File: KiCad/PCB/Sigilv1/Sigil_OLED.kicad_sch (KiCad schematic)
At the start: 13 parts, among them J2 INLAND 1.3" OLED HEADER (7-PI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, J3 BUZZER 2-PIN HEADER, J5 STATUS RING CABLE (JST-XH 3), SW1 UP (GPIO25, J11), SW2 DOWN (GPIO27, J9), SW3 LEFT (GPIO19, A12), SW4 RIGHT (GPIO21, A14), SW5 SELECT (GPIO32, J13), U1 REMOVABLE ESP32 DEVKIT / 2 x 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, U2 74AHCT1G125

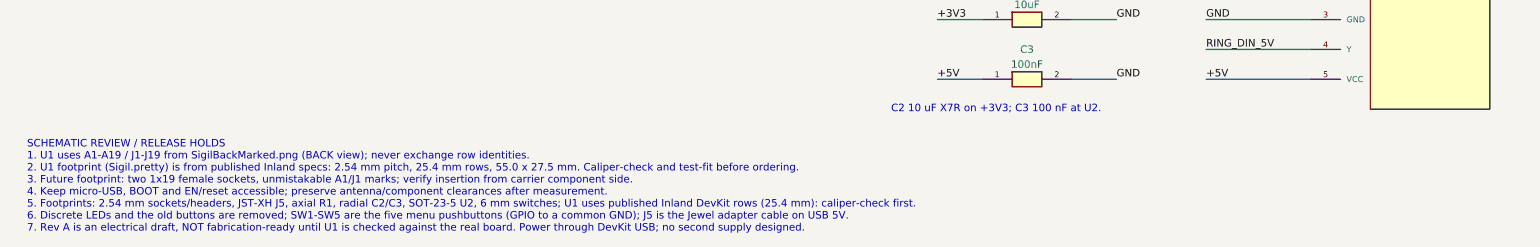
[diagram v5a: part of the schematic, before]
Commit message: Sigil U1 footprint: rows 22.86 mm, WROOM-32E, antenna keep-out
- The owner's Sigil DevKit straddles a standard breadboard with one free
  hole outside each row (columns b and i), so its rows are 22.86 mm
  (0.9 in) apart, not the published 25.4 mm. The footprint is renamed
  ESP32_DevKit_38_Socket_Row22.86mm; the 25.4 mm board is the wider
  30-pin DevKit on the test harness.
- Description names the ESP32-WROOM-32E module the boards actually carry.
- New 7 mm keep-out (no tracks, vias, pours or parts; socket pads allowed)
  over the antenna end past A19/J19. The depth is an estimate: measure it.
- Schematic release notes, README, CROSS_CHECK and the Prototype 1.0 gap
  review updated. KiCad 10.0.6 ERC: 0 violations on all three schematics;
  verify_schematic.py passes on exported netlists. Still Needs verification
  with calipers before ordering.

Co-Authored-By: Claude Opus 5.5 <noreply@anthropic.com>
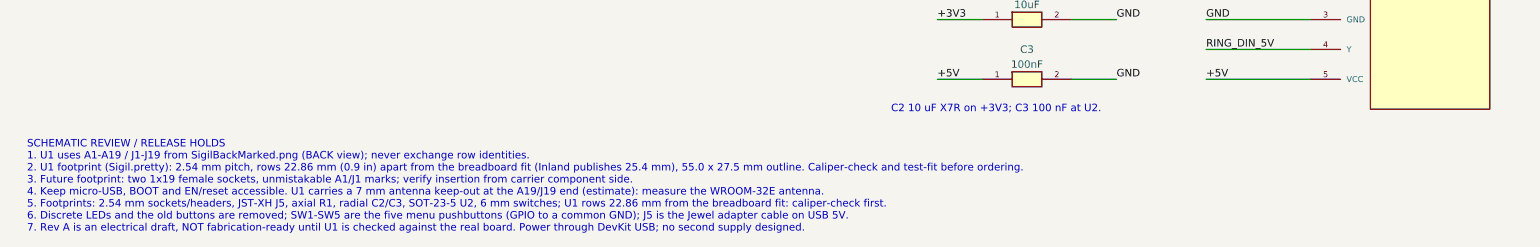
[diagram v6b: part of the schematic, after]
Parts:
- U1: footprint Sigil:ESP32_DevKit_38_Socket_Row25.4mm -> Sigil:ESP32_DevKit_38_Socket_Row22.86mm
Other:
- note added: "SCHEMATIC REVIEW / RELEASE HOLDS 1. U1 uses A1-A19 / J1-J19 from SigilBackMarked.png (BACK view); never exchange row identities. 2. U1 footprint (Sigil.pretty): 2.54 mm pitch, rows 22.86 mm (0.9 in) apart from the breadboard fit (Inland publishes 25.4 mm), 55.0 x 27.5 mm outline. Caliper-check and test-fit before ordering. 3. Future footprint: two 1x19 female sockets, unmistakable A1/J1 marks; ve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"
- note removed: "SCHEMATIC REVIEW / RELEASE HOLDS 1. U1 uses A1-A19 / J1-J19 from SigilBackMarked.png (BACK view); never exchange row identities. 2. U1 footprint (Sigil.pretty) is from published Inland specs: 2.54 mm pitch, 25.4 mm rows, 55.0 x 27.5 mm. Caliper-check and test-fit before ordering. 3. Future footprint: two 1x19 female sockets, unmistakable A1/J1 marks; verify insertion from carrier component side. 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"
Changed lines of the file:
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@@
 (title_block (title "Sigil Rev A - removable DevKit carrier, OLED display") (rev "A electrical draft") (comment 1 "Rear-photo socket numbering. Buttons SW1-SW5, status ring J5."))
 (symbol (lib_id "Sigil:ESP32_DevKit_38_RearReference") (at 88.9 101.6 0) (unit 1) (in_bom yes) (on_board yes) (dnp no)
- (property "Reference" "U1" (at 88.9 43.17999999999999 0)  (effects (font (size 1.27 1.27))))(property "Value" "REMOVABLE ESP32 DEVKIT / 2 x 19" (at 88.9 45.71999999999999 0)  (effects (font (size 1.27 1.27)))) (property "Footprint" "Sigil:ESP32_DevKit_38_Socket_Row25.4mm" (at 88.9 101.6 0) (hide yes) (effects (font (size 1.27 1.27)))) (pin "J1")(pin "J2")(pin "J3")(pin "J4")(pin "J5")(pin "J6")(pin "J7")(pin "J8")(pin "J9")(pin "J10")(pin "J11")(pin "J12")(pin "J13")(pin "J14")(pin "J15")(pin "J16")(pin "J17")(pin "J18")(pin "J19")(pin "A1")(pin "A2")(pin "A3")(pin "A4")(pin "A5")(pin "A6")(pin "A7")(pin "A8")(pin "A9")(pin "A10")(pin "A11")(pin "A12")(pin "A13")(pin "A14")(pin "A15")(pin "A16")(pin "A17")(pin "A18")(pin "A19")
+ (property "Reference" "U1" (at 88.9 43.17999999999999 0)  (effects (font (size 1.27 1.27))))(property "Value" "REMOVABLE ESP32 DEVKIT / 2 x 19" (at 88.9 45.71999999999999 0)  (effects (font (size 1.27 1.27)))) (property "Footprint" "Sigil:ESP32_DevKit_38_Socket_Row22.86mm" (at 88.9 101.6 0) (hide yes) (effects (font (size 1.27 1.27)))) (pin "J1")(pin "J2")(pin "J3")(pin "J4")(pin "J5")(pin "J6")(pin "J7")(pin "J8")(pin "J9")(pin "J10")(pin "J11")(pin "J12")(pin "J13")(pin "J14")(pin "J15")(pin "J16")(pin "J17")(pin "J18")(pin "J19")(pin "A1")(pin "A2")(pin "A3")(pin "A4")(pin "A5")(pin "A6")(pin "A7")(pin "A8")(pin "A9")(pin "A10")(pin "A11")(pin "A12")(pin "A13")(pin "A14")(pin "A15")(pin "A16")(pin "A17")(pin "A18")(pin "A19")
       (instances (project "Sigil_OLED" (path "/a61c2f0e-3b7d-4e55-9c1a-5d0e7b8f2c41" (reference "U1") (unit 1)))))
 (wire (pts (xy 45.72 55.88) (xy 25.4 55.88)) (stroke (width 0) (type default)))
@@
 (label "GND" (at 304.8 149.86 0) (effects (font (size 1.27 1.27)) (justify left bottom)))
 (text "J5: JST-XH 3-pin socket for the Jewel adapter pigtail\n(1 +5V, 2 DIN, 3 GND). The Jewel 7 RGBW and its bulk capacitor\nare on Sigil_JewelAdapter. 3.3 V data worked on the breadboard\nbut is below spec, so U2 (74AHCT1G125) buffers GPIO26 to 5 V;\nR1 (330 ohm) at the source damps the cable (the Jewel has its\nown 470 ohm on DIN). Full RGBW is ~560 mA, more than USB\nsupplies: firmware caps brightness at 48/255.\nDraws the status light (LedState); never the only signal." (at 290 160.02 0) (effects (font (size 1.27 1.27)) (justify left top)))
-(text "SCHEMATIC REVIEW / RELEASE HOLDS\n1. U1 uses A1-A19 / J1-J19 from SigilBackMarked.png (BACK view); never exchange row identities.\n2. U1 footprint (Sigil.pretty) is from published Inland specs: 2.54 mm pitch, 25.4 mm rows, 55.0 x 27.5 mm. Caliper-check and test-fit before ordering.\n3. Future footprint: two 1x19 female sockets, unmistakable A1/J1 marks; verify insertion from carrier component side.\n4. Keep micro-USB, BOOT and EN/reset accessible; preserve antenna/component clearances after measurement.\n5. Footprints: 2.54 mm sockets/headers, JST-XH J5, axial R1, radial C2/C3, SOT-23-5 U2, 6 mm switches; U1 uses published Inland DevKit rows (25.4 mm): caliper-check first.\n6. Discrete LEDs and the old buttons are removed; SW1-SW5 are the five menu pushbuttons (GPIO to a common GND); J5 is the Jewel adapter cable on USB 5V.\n7. Rev A is an electrical draft, NOT fabrication-ready until U1 is checked against the real board. Power through DevKit USB; no second supply designed." (at 28 211 0) (effects (font (size 1.27 1.27)) (justify left top)))
+(text "SCHEMATIC REVIEW / RELEASE HOLDS\n1. U1 uses A1-A19 / J1-J19 from SigilBackMarked.png (BACK view); never exchange row identities.\n2. U1 footprint (Sigil.pretty): 2.54 mm pitch, rows 22.86 mm (0.9 in) apart from the breadboard fit (Inland publishes 25.4 mm), 55.0 x 27.5 mm outline. Caliper-check and test-fit before ordering.\n3. Future footprint: two 1x19 female sockets, unmistakable A1/J1 marks; verify insertion from carrier component side.\n4. Keep micro-USB, BOOT and EN/reset accessible. U1 carries a 7 mm antenna keep-out at the A19/J19 end (estimate): measure the WROOM-32E antenna.\n5. Footprints: 2.54 mm sockets/headers, JST-XH J5, axial R1, radial C2/C3, SOT-23-5 U2, 6 mm switches; U1 rows 22.86 mm from the breadboard fit: caliper-check first.\n6. Discrete LEDs and the old buttons are removed; SW1-SW5 are the five menu pushbuttons (GPIO to a common GND); J5 is the Jewel adapter cable on USB 5V.\n7. Rev A is an electrical draft, NOT fabrication-ready until U1 is checked against the real board. Power through DevKit USB; no second supply designed." (at 28 211 0) (effects (font (size 1.27 1.27)) (justify left top)))
 (embedded_fonts no))
